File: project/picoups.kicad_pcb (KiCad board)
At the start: 4 copper layers, 65 x 30 mm, 74 parts, among them J1 VIN, J2 BATT, J3 USB_C_Receptacle, J4 Conn_02x20_Odd_Even, Q1 Q_PMOS_GSD, SW1 SW_5V, SW2 SW_USER, U1 LT3652EMSE, U2 TPS2116, U3 TPS61235P, U4 BQ24040, U5 INA3221, U6 M41T62

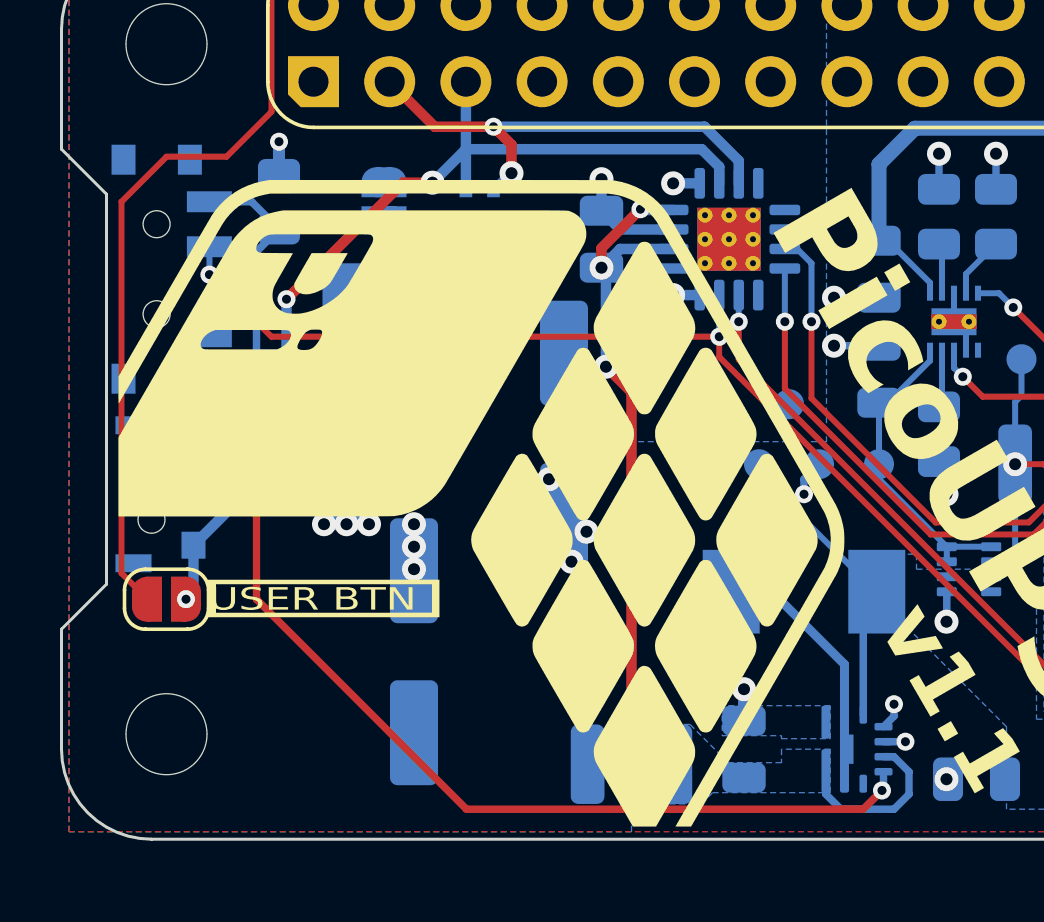
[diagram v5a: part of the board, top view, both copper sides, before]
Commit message: Moved main logo up a bit
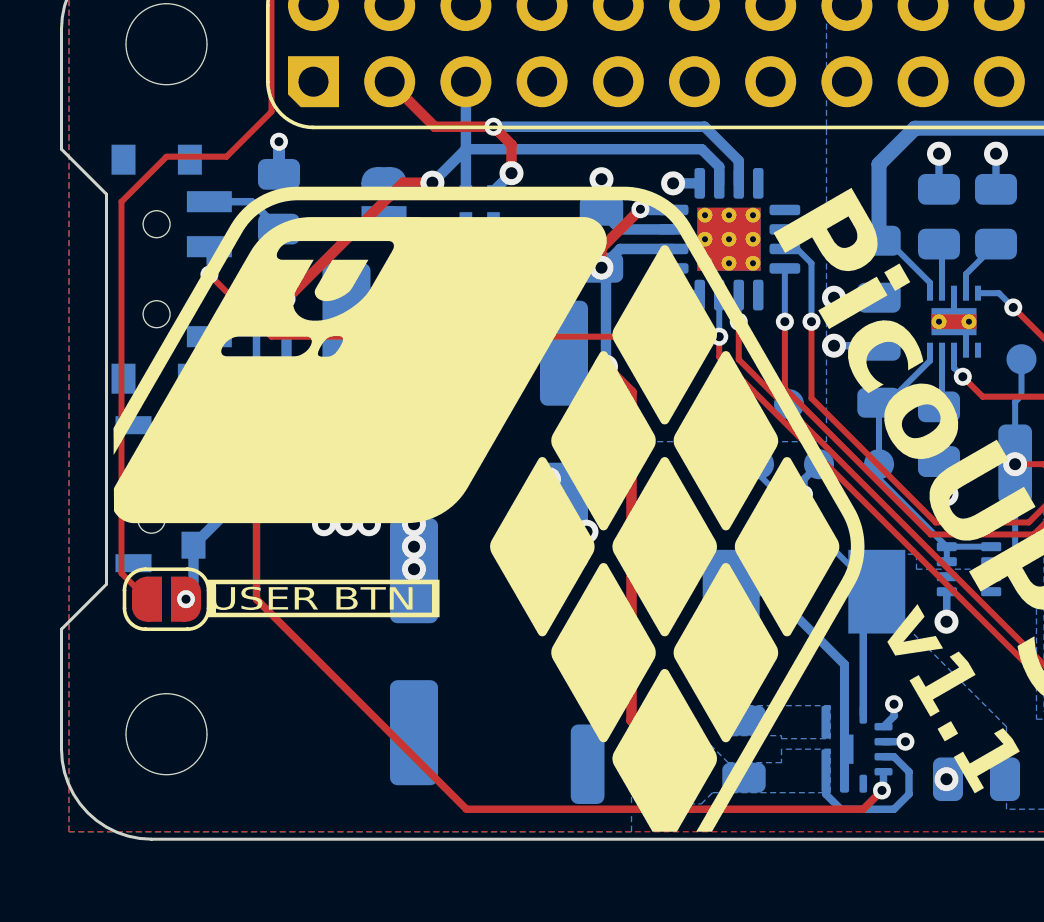
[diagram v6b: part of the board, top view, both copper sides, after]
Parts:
- removed G***: LOGO, PicoUPS:Logo_Front_Silk
- removed G***: LOGO, PicoUPS:Logo_Front_Mask
- added REF**: Logo_Front, PicoUPS:Logo_Front, F.Cu at (104.1, 112.2)

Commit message: Polishing touches~
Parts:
- moved C12 0.75 mm to (102.8, 116.5)
- moved C13 0.75 mm to (107.8, 109.2)
- moved C14 0.75 mm to (100.5, 108.0)
- moved JP6 0.25 mm to (102.0, 100.8)
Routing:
- net SCL: track 33.9 -> 32.5 mm
- net VBAT+: track 53.1 -> 52.2 mm
- net GND: track 42.0 -> 42.1 mm, vias 42 -> 78

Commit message: Revision 1.2.0
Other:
- board text added: "rev 1.2.0 16.09.23"
- board text added: "v1.2"
- board text removed: "rev 1.1.1 16.09.23"
- board text removed: "v1.1"
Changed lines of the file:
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@@
   (title_block
     (title "PicoUPS")
-    (date "2023-08-27")
-    (rev "1.1.0")
+    (date "2023-09-19")
+    (rev "1.2.0")
   )
   (layers
@@
     (effects (font (size 0.6 0.8) (thickness 0.15) bold) (justify mirror))
   )
-  (gr_text "rev 1.1.1\n16.09.23" (at 109.25 115) (layer "B.SilkS")
+  (gr_text "rev 1.2.0\n16.09.23" (at 109.25 115) (layer "B.SilkS")
     (effects (font (size 0.6 0.8) (thickness 0.15)) (justify mirror))
   )
@@
     (effects (font (size 0.75 1) (thickness 0.15)) (justify left))
   )
-  (gr_text "v1.1" (at 118 115 300) (layer "F.SilkS")
+  (gr_text "v1.2" (at 118 115 300) (layer "F.SilkS")
     (effects (font (size 2 2) (thickness 0.4) bold) (justify left bottom))
   )
